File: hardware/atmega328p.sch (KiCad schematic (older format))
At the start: 17 parts, among them J401 USART, U401 ATMEGA328P-PU, Y401 16MHz

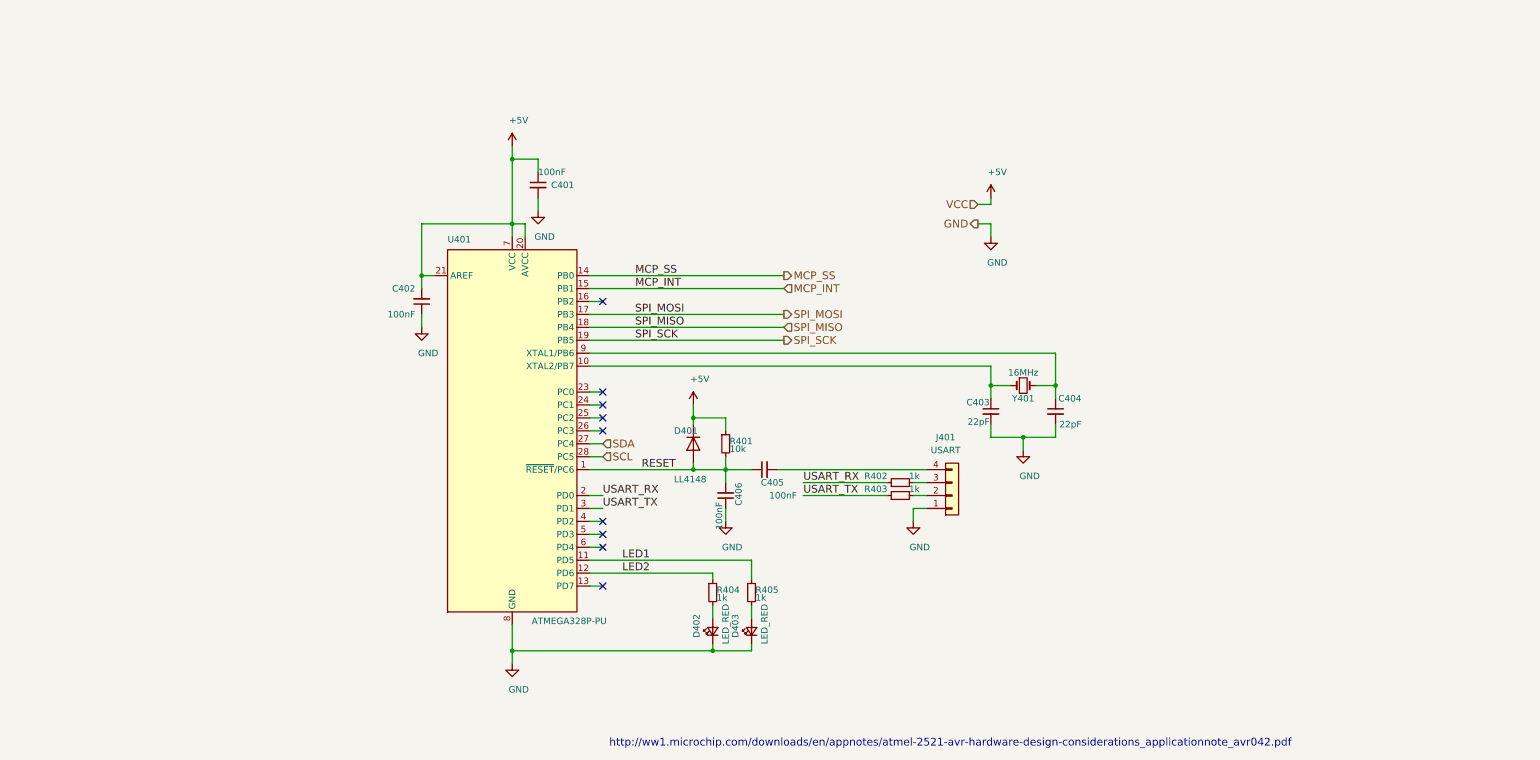
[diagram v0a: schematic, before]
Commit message: Subsubstituição do atmega pelo raspberry
No esquemático.
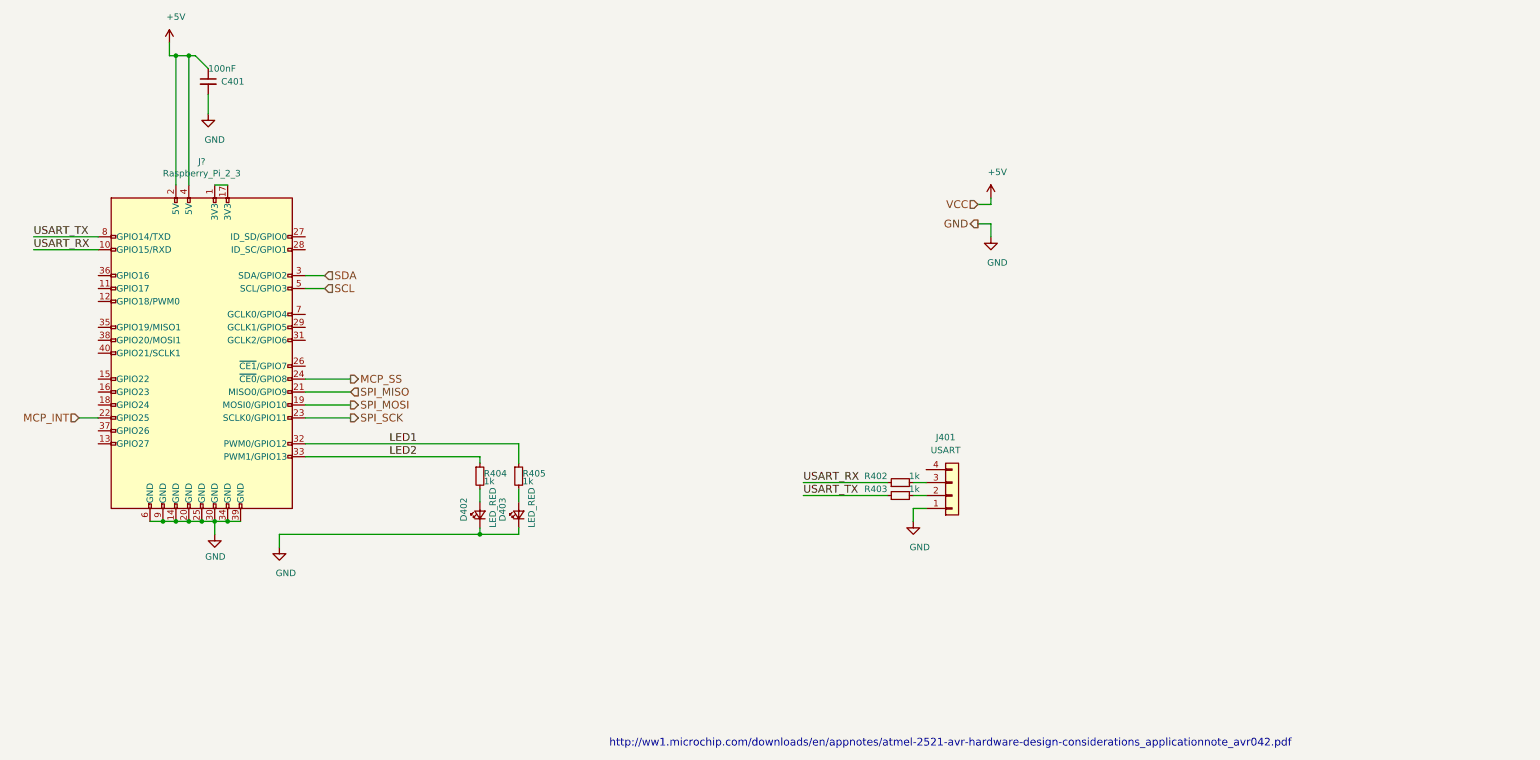
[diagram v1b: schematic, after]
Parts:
- removed C402, C405, C406: 100nF, Capacitor_SMD:C_0805_2012Metric_Pad1.15x1.40mm_HandSolder, symbol Device:C_Small
- removed C403, C404: 22pF, Capacitor_SMD:C_0805_2012Metric_Pad1.15x1.40mm_HandSolder, symbol Device:C_Small
- removed D401: LL4148, Diode_SMD:D_MiniMELF_Handsoldering, symbol Diode:LL4148
- removed R401: 10k, Resistor_SMD:R_0805_2012Metric_Pad1.15x1.40mm_HandSolder, symbol Device:R_Small
- removed U401: ATMEGA328P-PU, Package_DIP:DIP-28_W7.62mm_Socket, symbol basicsensormodule-rescue:ATmega328P-PU-MCU_Microchip_ATmega
- removed Y401: 16MHz, Crystal:Crystal_HC49-U_Vertical, symbol Device:Crystal_Small
- added J?: Raspberry_Pi_2_3, symbol Connector:Raspberry_Pi_2_3
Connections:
- net +5V: now also J?.2 (5V), J?.4 (5V)
- net GND: now also J?.14 (GND), J?.20 (GND), J?.25 (GND), J?.30 (GND), J?.34 (GND), J?.39 (GND), J?.6 (GND), J?.9 (GND)
- net LED1: now also J?.32 (PWM0/GPIO12)
- net LED2: now also J?.33 (PWM1/GPIO13)
- net MCP_INT: now also J?.22 (GPIO25)
- net MCP_SS: now also J?.24 (~CE0~/GPIO8)
- net SCL: now also J?.5 (SCL/GPIO3)
- net SDA: now also J?.3 (SDA/GPIO2)
- net SPI_MISO: now also J?.21 (MISO0/GPIO9)
- net SPI_MOSI: now also J?.19 (MOSI0/GPIO10)
- net SPI_SCK: now also J?.23 (SCLK0/GPIO11)
- net USART_RX: now also J?.10 (GPIO15/RXD)
- net USART_TX: now also J?.8 (GPIO14/TXD)
- new net: J?.1 (3V3), J?.17 (3V3)
- no-connect marks 9 -> 0
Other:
- moved on the sheet: C401, D402, D403, R404, R405

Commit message: Adicão da alimentação de uma folha para outra .
Alimentação de 3V3.
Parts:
- gave numbers to parts that had none: 1
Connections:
- net 3V3: now reaches J501.1 (3V3), J501.17 (3V3)
- no-connect marks 0 -> 18
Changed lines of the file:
@@
 $Descr A4 11693 8268
 encoding utf-8
-Sheet 3 5
+Sheet 5 5
 Title ""
 Date ""
@@
 $EndComp
 Wire Wire Line
-	2000 1150 1900 1050
-Wire Wire Line
 	1700 1050 1700 950
-Wire Wire Line
-	1900 1050 1850 1050
 $Comp
 L power:GND #PWR0403
@@
 SDA
 $Comp
-L Connector:Raspberry_Pi_2_3 J?
+L Connector:Raspberry_Pi_2_3 J501
 U 1 1 5CD265D6
 P 1950 3350
-F 0 "J?" H 1950 4831 50  0000 C CNN
+F 0 "J501" H 1950 4831 50  0000 C CNN
 F 1 "Raspberry_Pi_2_3" H 1950 4740 50  0000 C CNN
 F 2 "" H 1950 3350 50  0001 C CNN
@@
 	2000 1500 2000 1350
 Wire Wire Line
-	2050 2050 2150 2050
+	2050 2050 2100 2050
 Wire Wire Line
 	1550 4650 1650 4650
@@
 	2150 4650 2250 4650
 $Comp
-L power:GND #PWR?
+L power:GND #PWR0501
 U 1 1 5CD43A1C
 P 2050 4750
-F 0 "#PWR?" H 2050 4500 50  0001 C CNN
+F 0 "#PWR0501" H 2050 4500 50  0001 C CNN
 F 1 "GND" H 2055 4577 50  0000 C CNN
 F 2 "" H 2050 4750 50  0001 C CNN
@@
 Wire Wire Line
 	2750 4150 4100 4150
+Text HLabel 2550 1950 2    50   Input ~ 0
+3V3
+Wire Wire Line
+	2550 1950 2450 1950
+Wire Wire Line
+	2100 1950 2100 2050
+Connection ~ 2100 2050
+Wire Wire Line
+	2100 2050 2150 2050
+NoConn ~ 1150 4050
+NoConn ~ 1150 3950
+NoConn ~ 1150 3650
+NoConn ~ 1150 3550
+NoConn ~ 1150 3750
+NoConn ~ 1150 3250
+NoConn ~ 1150 3350
+NoConn ~ 1150 3150
+NoConn ~ 1150 2950
+NoConn ~ 1150 2850
+NoConn ~ 1150 2750
+NoConn ~ 2750 2550
+NoConn ~ 2750 2450
+NoConn ~ 2750 3050
+NoConn ~ 2750 3150
+NoConn ~ 2750 3250
+NoConn ~ 2750 3450
+$Comp
+L power:PWR_FLAG #FLG0101
+U 1 1 5CD6B837
+P 2450 1900
+F 0 "#FLG0101" H 2450 1975 50  0001 C CNN
+F 1 "PWR_FLAG" H 2450 2073 50  0000 C CNN
+F 2 "" H 2450 1900 50  0001 C CNN
+F 3 "~" H 2450 1900 50  0001 C CNN
+	1    2450 1900
+	1    0    0    -1
+$EndComp
+Wire Wire Line
+	2450 1900 2450 1950
+Connection ~ 2450 1950
+Wire Wire Line
+	2450 1950 2100 1950
+NoConn ~ 7550 4250
+Wire Wire Line
+	1850 1050 2000 1050
+Wire Wire Line
+	2000 1150 2000 1050
 $EndSCHEMATC

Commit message: PCB atualizada com as mudanças do raspberry
Foram adicionadas as mudanças do conector do raspberry e retirado algumas coisas não necessárias.
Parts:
- J501: footprint (none) -> Connector_PinHeader_2.54mm:PinHeader_2x20_P2.54mm_Vertical
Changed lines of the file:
@@
 F 0 "J501" H 1950 4831 50  0000 C CNN
 F 1 "Raspberry_Pi_2_3" H 1950 4740 50  0000 C CNN
-F 2 "" H 1950 3350 50  0001 C CNN
+F 2 "Connector_PinHeader_2.54mm:PinHeader_2x20_P2.54mm_Vertical" H 1950 3350 50  0001 C CNN
 F 3 "https://www.raspberrypi.org/documentation/hardware/raspberrypi/schematics/rpi_SCH_3bplus_1p0_reduced.pdf" H 1950 3350 50  0001 C CNN
 	1    1950 3350

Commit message: Project cleaned
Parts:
- removed J401: USART, Connector_PinHeader_2.54mm:PinHeader_1x04_P2.54mm_Vertical, symbol Connector_Generic:Conn_01x04
- removed R402, R403: 1k, Resistor_SMD:R_0805_2012Metric_Pad1.15x1.40mm_HandSolder, symbol Device:R_Small
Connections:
- no-connect marks 18 -> 17
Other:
- note removed: "http://ww1.microchip.com/downloads/en/appnotes/atmel-2521-avr-hardware-design-considerations_applicationnote_avr042.pdf"
- moved on the sheet: C401, D402, D403, J501, R404, R405
